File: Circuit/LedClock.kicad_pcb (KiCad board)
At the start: 2 copper layers, 86.3 x 49.7 mm, 24 parts, among them K1 PROG, SW1 MSP_RESET, U1 MSP430G2553IPW20

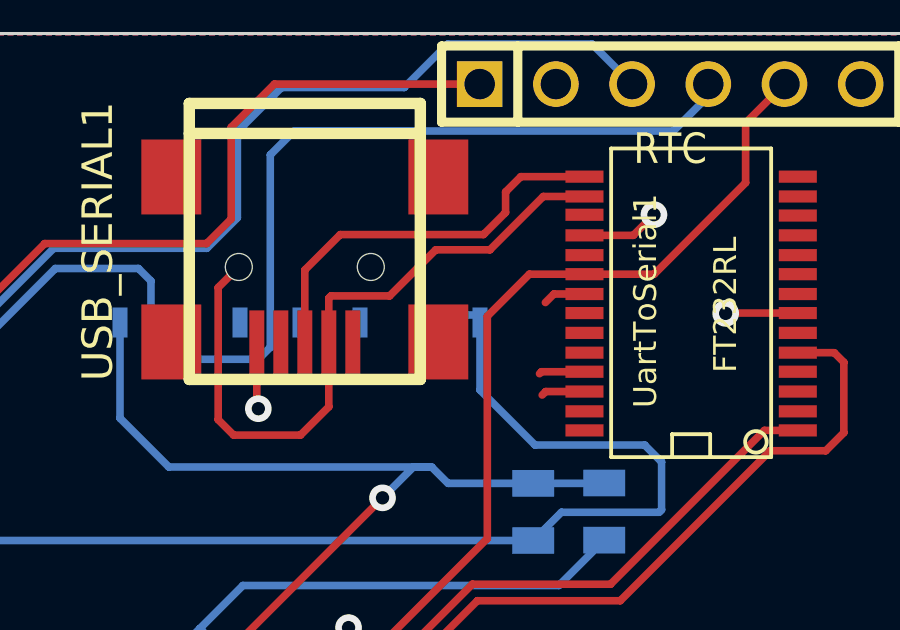
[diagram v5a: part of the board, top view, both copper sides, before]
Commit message: Updated pcb layout and circuit, found 1 flaw in the design
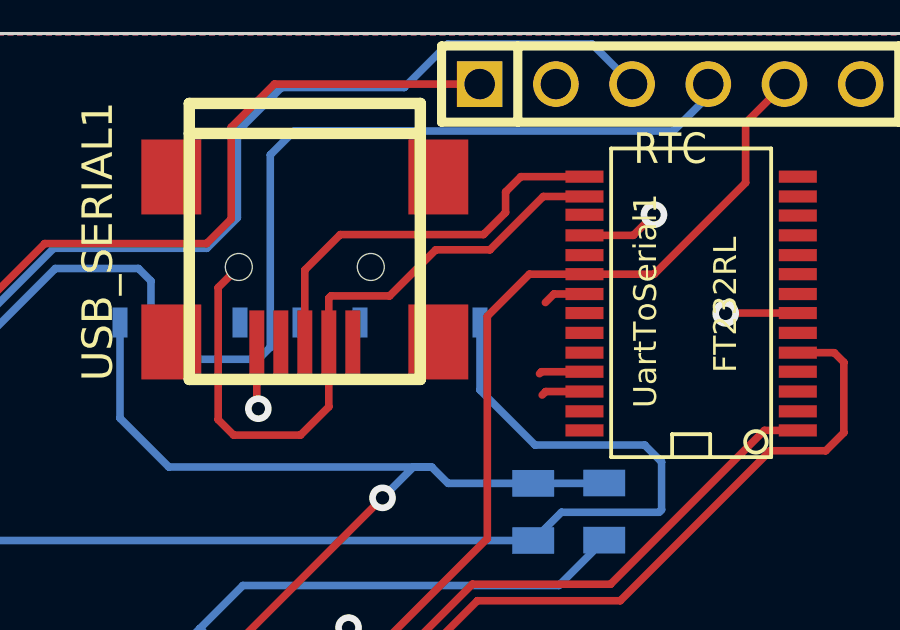
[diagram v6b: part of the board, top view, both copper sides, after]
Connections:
- ESP1 pad 13: N-0000015 -> (no net)
- ESP1 pad 14: N-0000015 -> N-0000014
- R46K2 pad 2: N-0000015 -> N-0000014
- SWProg1 pad 1: N-0000015 -> N-0000014
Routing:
- net N-0000015: track 47.4 -> 0.00 mm
- net N-0000014: track 0.00 -> 45.4 mm
